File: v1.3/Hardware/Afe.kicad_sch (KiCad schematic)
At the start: 38 parts, among them U10 ACPL-7900, U13 L78L05_SOT89, U3 MCP6024, U4 ACPL-7900

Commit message: Serial interface development. Manual added. Untested.
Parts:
- removed R10: 1k %1, Resistor_SMD:R_0805_2012Metric, symbol Device:R_Small
- added R?: 10R %1, Resistor_SMD:R_0805_2012Metric, symbol Device:R_Small
- C44: value 470p %5 -> 47n %5; footprint Capacitor_SMD:C_0805_2012Metric -> Capacitor_SMD:C_1206_3216Metric; Link https://ozdisan.com/passive-components/capacitors/smt-smd-and-mlcc-capacitors/CL21C471JBANNNC -> https://ozdisan.com/passive-components/capacitors/smt-smd-and-mlcc-capacitors/CL31B473JBCNNNC; Price 0.01305 USD -> 0.03867 USD
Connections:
- net VDIV: now also R?.2
- net at C44.1, U10.2 (IN+): now also R?.1
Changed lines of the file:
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@@
-(kicad_sch (version 20200714) (host eeschema "5.99.0-unknown-4b7c88309~102~ubuntu18.04.1")
-  (page 2 7)
+(kicad_sch (version 20201015) (generator eeschema)
+  (page 1 7)
   (paper "A4")
   (junction (at 96.52 59.69) (diameter 0.3048) (color 0 0 0 0))
@@
     )
   )
-  (symbol (lib_name "Device:R_Small_10") (lib_id "Device:R_Small") (at 167.005 59.69 90) (unit 1)
-    (in_bom yes) (on_board yes)
-    (property "Reference" "R10" (id 0) (at 167.005 54.7432 90))
-    (property "Value" "1k %1" (id 1) (at 167.005 57.0419 90))
-    (property "Footprint" "Resistor_SMD:R_0805_2012Metric" (id 2) (at 167.005 57.042 90)
+  (symbol (lib_name "Device:R_Small_3") (lib_id "Device:R_Small") (at 167.005 59.69 90) (unit 1)
+    (in_bom yes) (on_board yes)
+    (property "Reference" "R?" (id 0) (at 167.005 61.595 90))
+    (property "Value" "10R %1" (id 1) (at 167.005 57.785 90))
+    (property "Footprint" "Resistor_SMD:R_0805_2012Metric" (id 2) (at 167.005 59.69 0)
       (effects (font (size 1.27 1.27)) hide)
     )
@@
       (effects (font (size 1.27 1.27)) hide)
     )
-    (property "Link" "https://ozdisan.com/passive-components/resistors/smt-smd-and-chip-resistors/0805S8F1001T5E" (id 4) (at 167.005 59.69 90)
-      (effects (font (size 1.27 1.27)) hide)
-    )
-    (property "Price" "0.00286 USD" (id 5) (at 167.005 59.69 90)
+    (property "Link" "https://ozdisan.com/passive-components/resistors/smt-smd-and-chip-resistors/TC0550F100JT5F" (id 4) (at 167.005 59.69 90)
+      (effects (font (size 1.27 1.27)) hide)
+    )
+    (property "Price" "0.02574 USD" (id 5) (at 167.005 59.69 90)
       (effects (font (size 1.27 1.27)) hide)
     )
@@
     )
   )
-  (symbol (lib_name "Device:C_Small_12") (lib_id "Device:C_Small") (at 163.195 64.77 0) (unit 1)
+  (symbol (lib_name "Device:C_Small_2") (lib_id "Device:C_Small") (at 163.195 64.77 0) (unit 1)
     (in_bom yes) (on_board yes)
     (property "Reference" "C44" (id 0) (at 159.385 64.77 0)
       (effects (font (size 1.27 1.27)) (justify left))
     )
-    (property "Value" "470p %5" (id 1) (at 165.1 63.5 0)
-      (effects (font (size 1.27 1.27)) (justify left))
-    )
-    (property "Footprint" "Capacitor_SMD:C_0805_2012Metric" (id 2) (at 163.195 64.77 0)
+    (property "Value" "47n %5" (id 1) (at 165.1 63.5 0)
+      (effects (font (size 1.27 1.27)) (justify left))
+    )
+    (property "Footprint" "Capacitor_SMD:C_1206_3216Metric" (id 2) (at 163.195 64.77 0)
       (effects (font (size 1.27 1.27)) hide)
     )
@@
       (effects (font (size 1.27 1.27)) hide)
     )
-    (property "Link" "https://ozdisan.com/passive-components/capacitors/smt-smd-and-mlcc-capacitors/CL21C471JBANNNC" (id 4) (at 163.195 64.77 0)
-      (effects (font (size 1.27 1.27)) hide)
-    )
-    (property "Price" "0.01305 USD" (id 5) (at 163.195 64.77 0)
-      (effects (font (size 1.27 1.27)) hide)
-    )
+    (property "Link" "https://ozdisan.com/passive-components/capacitors/smt-smd-and-mlcc-capacitors/CL31B473JBCNNNC" (id 4) (at 163.195 64.77 0)
+      (effects (font (size 1.27 1.27)) hide)
+    )
+    (property "Price" "0.03867 USD" (id 5) (at 163.195 64.77 0)
+      (effects (font (size 1.27 1.27)) hide)
+    )

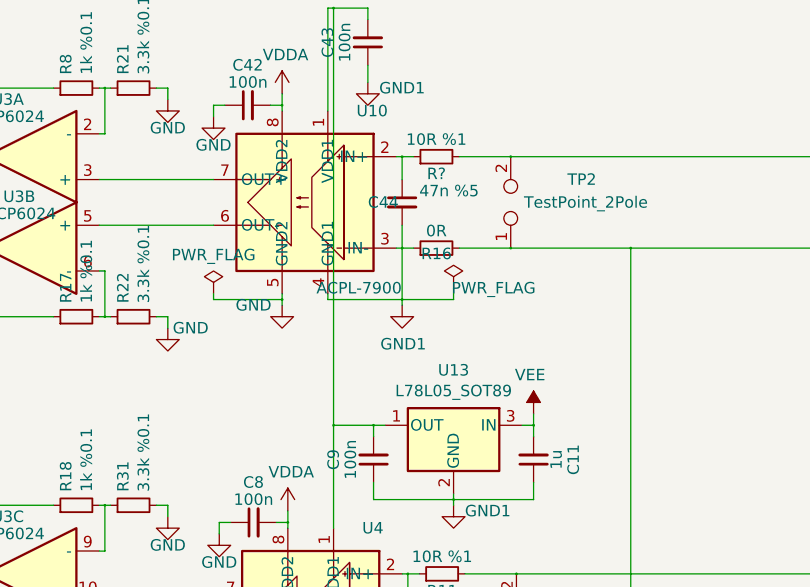
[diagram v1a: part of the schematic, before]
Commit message: v1.3 Schematic, footprints and BOM updated.
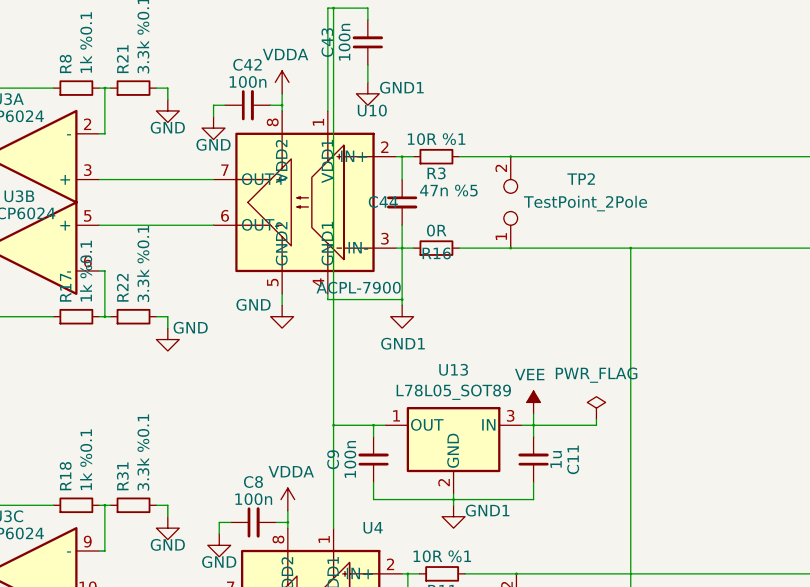
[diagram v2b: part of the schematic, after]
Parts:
- C4, C41, C6, C7: Link (none) -> https://ozdisan.com/passive-components/capacitors/smt-smd-a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; Price (none) -> 0.01610 USD
- gave numbers to parts that had none: 1
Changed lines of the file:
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@@
   (junction (at 130.175 123.825) (diameter 0.3048) (color 0 0 0 0))
   (junction (at 149.86 53.975) (diameter 0.3048) (color 0 0 0 0))
-  (junction (at 149.86 75.565) (diameter 0.3048) (color 0 0 0 0))
   (junction (at 150.495 100.33) (diameter 0.3048) (color 0 0 0 0))
   (junction (at 150.495 121.92) (diameter 0.3048) (color 0 0 0 0))
@@
     (stroke (width 0) (type solid) (color 0 0 0 0))
   )
-  (wire (pts (xy 142.24 74.93) (xy 142.24 75.565))
-    (stroke (width 0) (type solid) (color 0 0 0 0))
-  )
-  (wire (pts (xy 142.24 75.565) (xy 149.86 75.565))
-    (stroke (width 0) (type solid) (color 0 0 0 0))
-  )
   (wire (pts (xy 142.875 100.33) (xy 144.145 100.33))
     (stroke (width 0) (type solid) (color 0 0 0 0))
@@
     (stroke (width 0) (type solid) (color 0 0 0 0))
   )
-  (wire (pts (xy 149.86 74.93) (xy 149.86 75.565))
-    (stroke (width 0) (type solid) (color 0 0 0 0))
-  )
-  (wire (pts (xy 149.86 75.565) (xy 149.86 76.2))
+  (wire (pts (xy 149.86 74.93) (xy 149.86 76.2))
     (stroke (width 0) (type solid) (color 0 0 0 0))
   )
@@
     (stroke (width 0) (type solid) (color 0 0 0 0))
   )
-  (wire (pts (xy 163.195 75.565) (xy 168.91 75.565))
-    (stroke (width 0) (type solid) (color 0 0 0 0))
-  )
   (wire (pts (xy 163.195 106.045) (xy 163.83 106.045))
     (stroke (width 0) (type solid) (color 0 0 0 0))
@@
     (stroke (width 0) (type solid) (color 0 0 0 0))
   )
-  (wire (pts (xy 168.91 75.565) (xy 168.91 74.295))
-    (stroke (width 0) (type solid) (color 0 0 0 0))
-  )
   (wire (pts (xy 168.91 97.155) (xy 168.91 97.79))
     (stroke (width 0) (type solid) (color 0 0 0 0))
@@
     (stroke (width 0) (type solid) (color 0 0 0 0))
   )
+  (wire (pts (xy 177.8 89.535) (xy 184.785 89.535))
+    (stroke (width 0) (type solid) (color 0 0 0 0))
+  )
   (wire (pts (xy 177.8 90.805) (xy 177.8 89.535))
     (stroke (width 0) (type solid) (color 0 0 0 0))
@@
   )
   (wire (pts (xy 177.8 97.79) (xy 168.91 97.79))
+    (stroke (width 0) (type solid) (color 0 0 0 0))
+  )
+  (wire (pts (xy 184.785 88.9) (xy 184.785 89.535))
     (stroke (width 0) (type solid) (color 0 0 0 0))
   )
@@
     (effects (font (size 1.27 1.27)) (justify left))
   )
-  (symbol (lib_name "power:PWR_FLAG_2") (lib_id "power:PWR_FLAG") (at 142.24 74.93 0) (unit 1)
-    (in_bom yes) (on_board yes)
-    (property "Reference" "#FLG0111" (id 0) (at 142.24 73.025 0)
-      (effects (font (size 1.27 1.27)) hide)
-    )
-    (property "Value" "PWR_FLAG" (id 1) (at 142.24 70.612 0))
-    (property "Footprint" "" (id 2) (at 142.24 74.93 0)
-      (effects (font (size 1.27 1.27)) hide)
-    )
-    (property "Datasheet" "~" (id 3) (at 142.24 74.93 0)
-      (effects (font (size 1.27 1.27)) hide)
-    )
-  )
   (symbol (lib_id "power:PWR_FLAG") (at 142.875 121.285 0) (unit 1)
     (in_bom yes) (on_board yes)
@@
     )
   )
-  (symbol (lib_name "power:PWR_FLAG_1") (lib_id "power:PWR_FLAG") (at 168.91 74.295 0) (unit 1)
-    (in_bom yes) (on_board yes)
-    (property "Reference" "#FLG0112" (id 0) (at 168.91 72.39 0)
-      (effects (font (size 1.27 1.27)) hide)
-    )
-    (property "Value" "PWR_FLAG" (id 1) (at 173.355 74.295 0))
-    (property "Footprint" "" (id 2) (at 168.91 74.295 0)
-      (effects (font (size 1.27 1.27)) hide)
-    )
-    (property "Datasheet" "~" (id 3) (at 168.91 74.295 0)
-      (effects (font (size 1.27 1.27)) hide)
-    )
-  )
   (symbol (lib_id "power:PWR_FLAG") (at 169.545 120.65 0) (unit 1)
     (in_bom yes) (on_board yes)
@@
     )
     (property "Datasheet" "~" (id 3) (at 169.545 120.65 0)
+      (effects (font (size 1.27 1.27)) hide)
+    )
+  )
+  (symbol (lib_name "power:PWR_FLAG_2") (lib_id "power:PWR_FLAG") (at 184.785 88.9 0) (unit 1)
+    (in_bom yes) (on_board yes)
+    (property "Reference" "#FLG0111" (id 0) (at 184.785 86.995 0)
+      (effects (font (size 1.27 1.27)) hide)
+    )
+    (property "Value" "PWR_FLAG" (id 1) (at 184.785 83.82 0))
+    (property "Footprint" "" (id 2) (at 184.785 88.9 0)
+      (effects (font (size 1.27 1.27)) hide)
+    )
+    (property "Datasheet" "~" (id 3) (at 184.785 88.9 0)
       (effects (font (size 1.27 1.27)) hide)
     )
@@
   (symbol (lib_name "Device:R_Small_3") (lib_id "Device:R_Small") (at 167.005 59.69 90) (unit 1)
     (in_bom yes) (on_board yes)
-    (property "Reference" "R?" (id 0) (at 167.005 61.595 90))
+    (property "Reference" "R3" (id 0) (at 167.005 61.595 90))
     (property "Value" "10R %1" (id 1) (at 167.005 57.785 90))
     (property "Footprint" "Resistor_SMD:R_0805_2012Metric" (id 2) (at 167.005 59.69 0)
@@
       (effects (font (size 1.27 1.27)) hide)
     )
+    (property "Link" "https://ozdisan.com/passive-components/capacitors/smt-smd-and-mlcc-capacitors/CL21C102JBCNNNC" (id 4) (at 102.87 55.245 0)
+      (effects (font (size 1.27 1.27)) hide)
+    )
+    (property "Price" "0.01610 USD" (id 5) (at 102.87 55.245 0)
+      (effects (font (size 1.27 1.27)) hide)
+    )
   )
   (symbol (lib_name "Device:C_Small_16") (lib_id "Device:C_Small") (at 102.87 64.77 0) (unit 1)
@@
       (effects (font (size 1.27 1.27)) hide)
     )
+    (property "Link" "https://ozdisan.com/passive-components/capacitors/smt-smd-and-mlcc-capacitors/CL21C102JBCNNNC" (id 4) (at 102.87 73.025 0)
+      (effects (font (size 1.27 1.27)) hide)
+    )
+    (property "Price" "0.01610 USD" (id 5) (at 102.87 73.025 0)
+      (effects (font (size 1.27 1.27)) hide)
+    )
   )
   (symbol (lib_name "Device:C_Small_17") (lib_id "Device:C_Small") (at 102.87 101.6 0) (unit 1)
@@
       (effects (font (size 1.27 1.27)) hide)
     )
+    (property "Link" "https://ozdisan.com/passive-components/capacitors/smt-smd-and-mlcc-capacitors/CL21C102JBCNNNC" (id 4) (at 102.87 101.6 0)
+      (effects (font (size 1.27 1.27)) hide)
+    )
+    (property "Price" "0.01610 USD" (id 5) (at 102.87 101.6 0)
+      (effects (font (size 1.27 1.27)) hide)
+    )
   )
   (symbol (lib_name "Device:C_Small_19") (lib_id "Device:C_Small") (at 102.87 111.125 0) (unit 1)
@@
       (effects (font (size 1.27 1.27)) hide)
     )
+    (property "Link" "https://ozdisan.com/passive-components/capacitors/smt-smd-and-mlcc-capacitors/CL21C102JBCNNNC" (id 4) (at 102.87 119.38 0)
+      (effects (font (size 1.27 1.27)) hide)
+    )
+    (property "Price" "0.01610 USD" (id 5) (at 102.87 119.38 0)
+      (effects (font (size 1.27 1.27)) hide)
+    )
